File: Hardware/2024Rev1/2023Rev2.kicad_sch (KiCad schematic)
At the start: 91 parts, among them J2 Conn_01x03, J3 Conn_01x03, J4 Conn_01x02, J5 Conn_01x09, J6 Conn_01x09, J7 RJ45_LED_Shielded, J9 Conn_01x04, Q2 Q_NMOS_DGS, Q3 Q_NMOS_DGS, Q4 Q_NMOS_DGS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

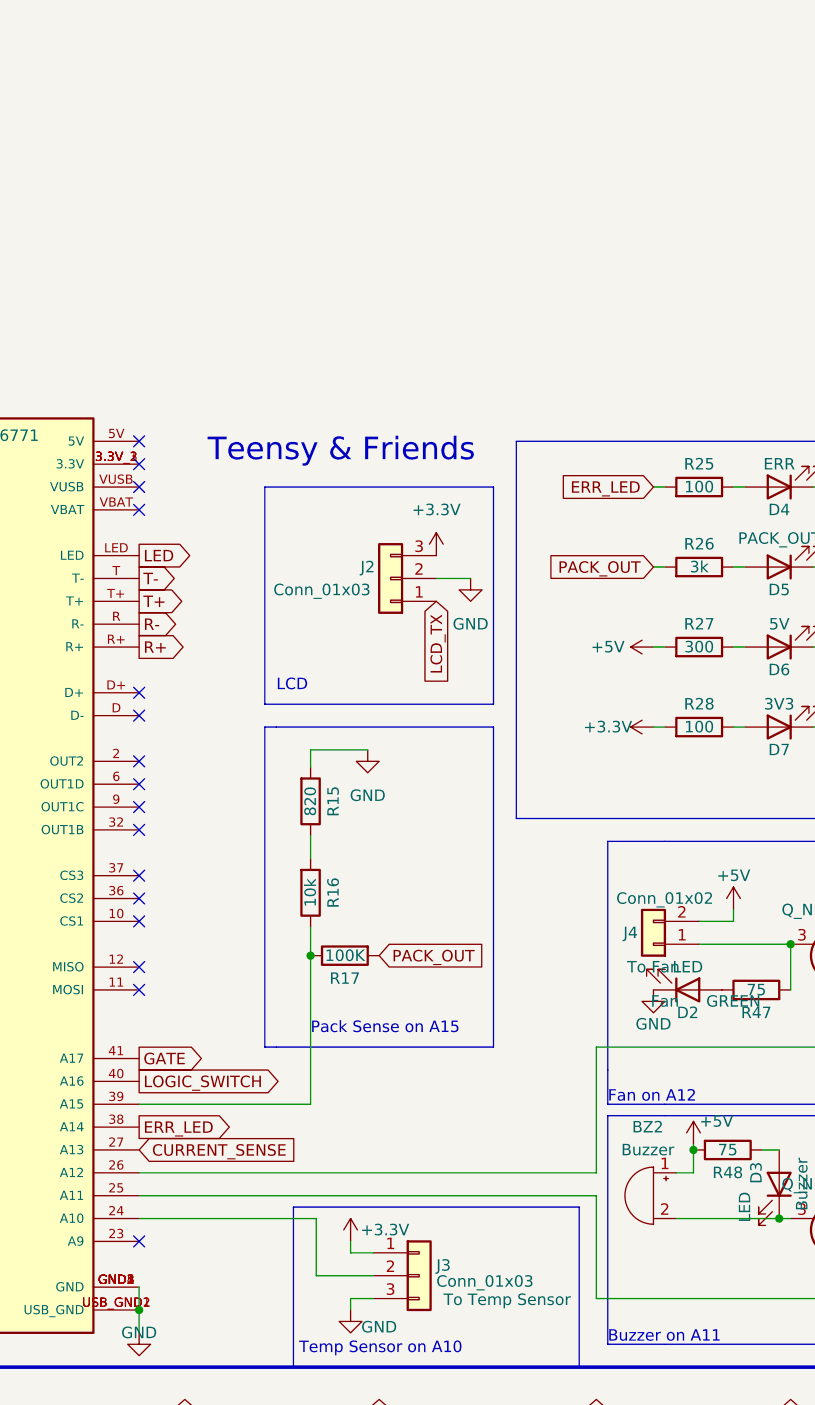
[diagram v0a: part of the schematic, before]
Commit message: added in molex
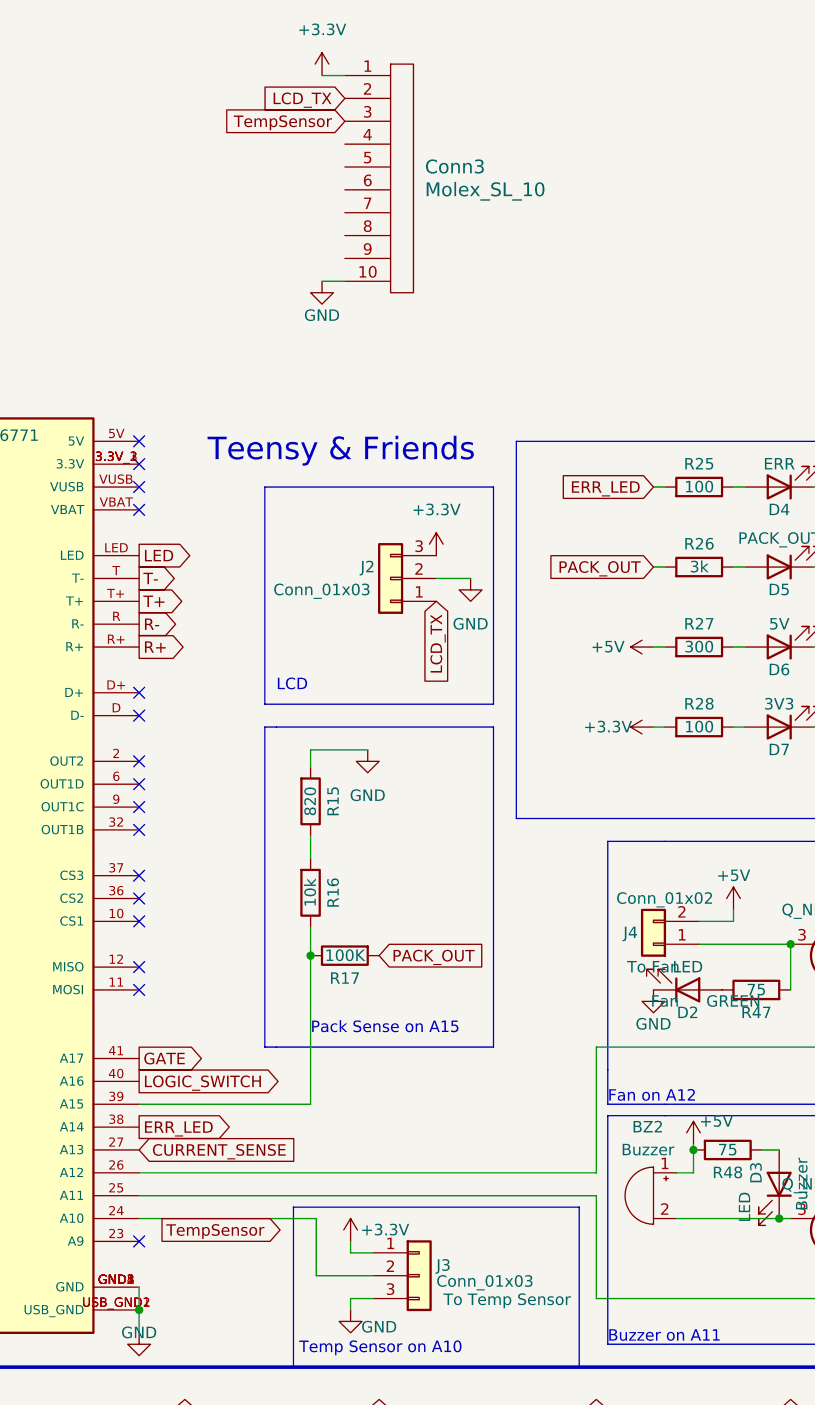
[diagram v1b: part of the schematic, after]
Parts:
- added Conn3: Molex_SL_10, symbol MRDT_Connectors:Molex_SL_10
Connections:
- net +3.3V: now also Conn3.1
- net GND: now also Conn3.10
- net LCD_TX: now also Conn3.2
- new net TempSensor: Conn3.3
